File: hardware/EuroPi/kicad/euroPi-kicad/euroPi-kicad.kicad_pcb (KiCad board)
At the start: 2 copper layers, 121.9 x 128.5 mm, 104 parts, among them J1 Output 1 Jack, J10 Eurorack Power 2x8 16p, J11 Conn_01x13_Socket, J12 OLED 64x128, J13 USB_B_Micro, J14 Conn_01x03_Pin, J15 Conn_01x04_Pin, J16 Conn_02x04_Top_Bottom, J17 Conn_01x13_Pin, J18 Conn_01x04_Pin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

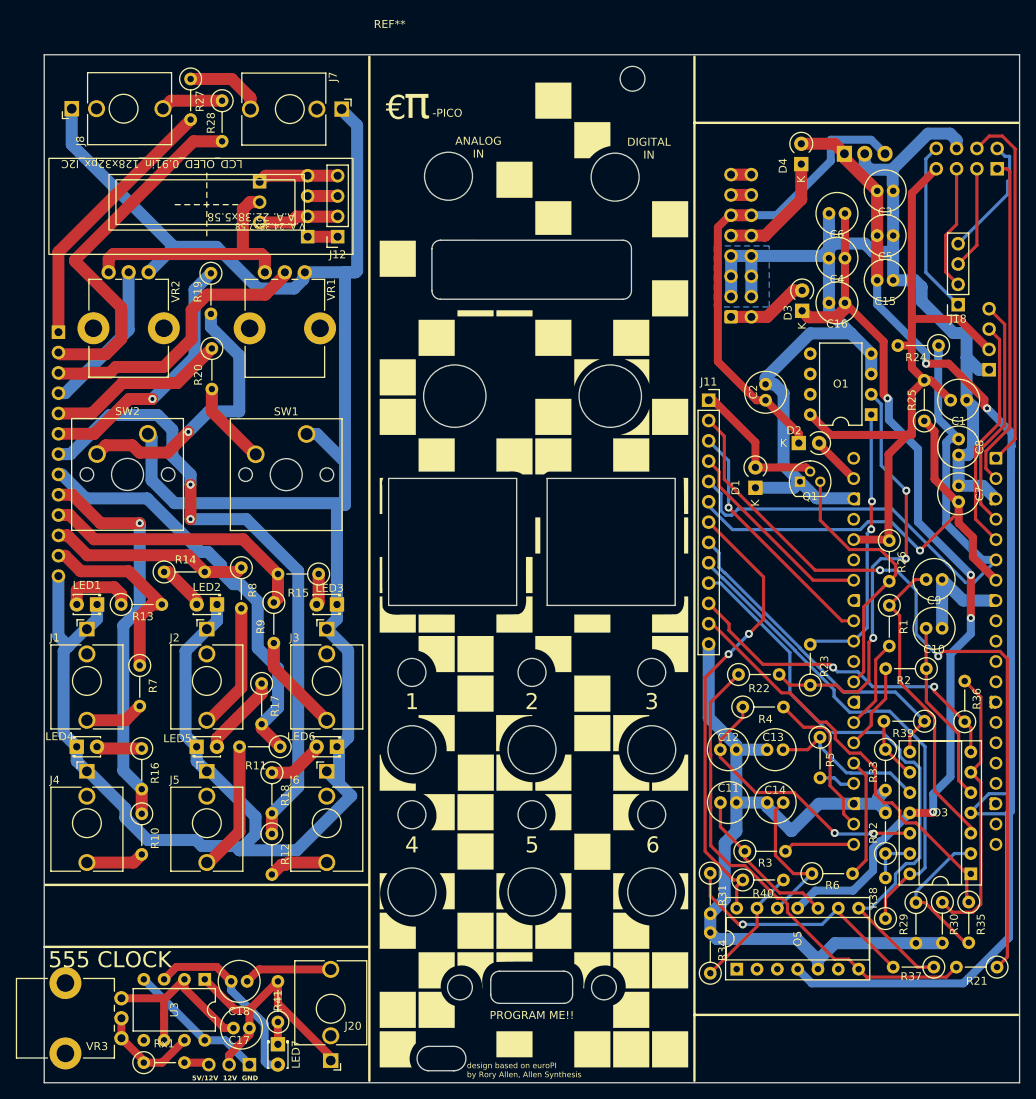
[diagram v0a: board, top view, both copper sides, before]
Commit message: euroPI base minor fixes incl adding ground plane
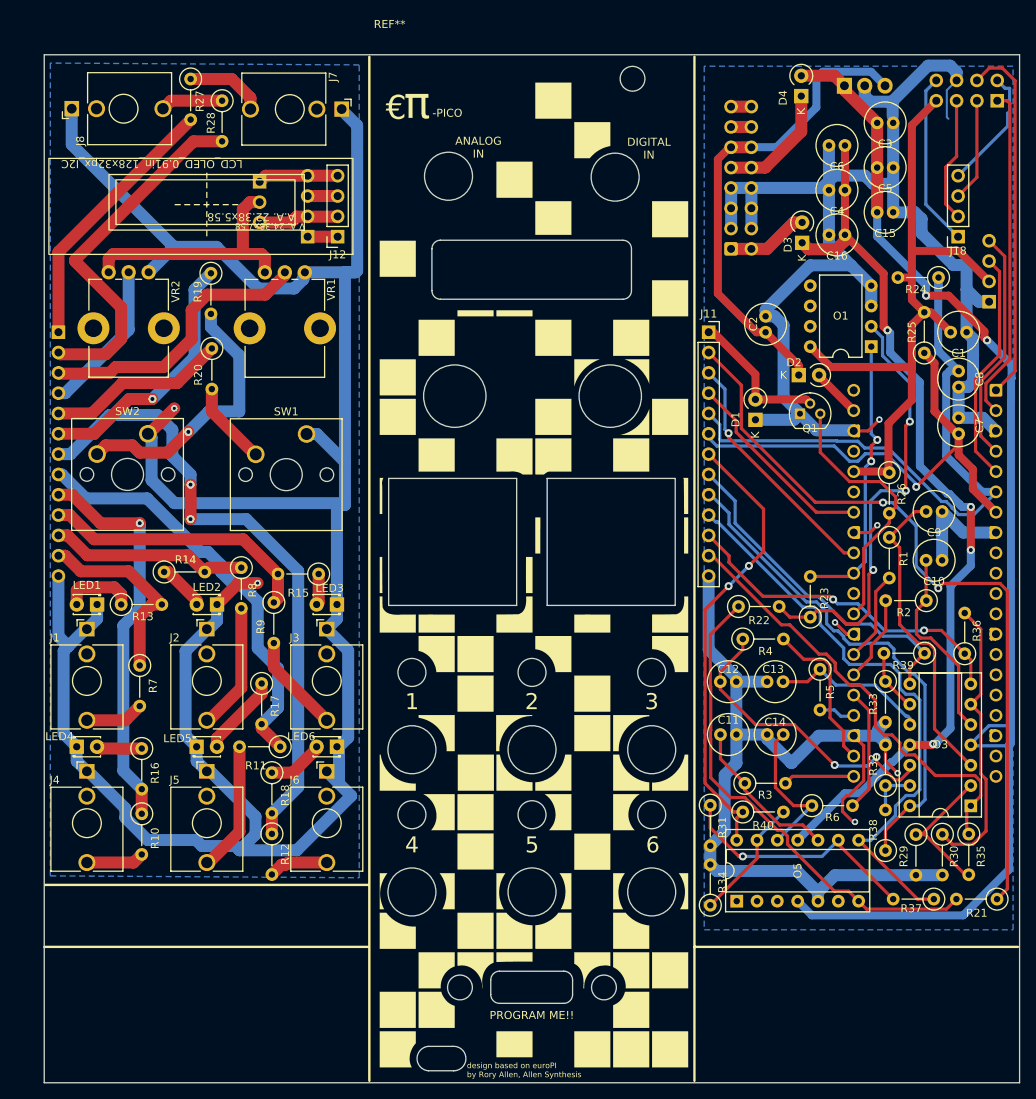
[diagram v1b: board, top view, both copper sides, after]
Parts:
- removed C17: 1uF, Capacitor_THT:C_Radial_D5.0mm_H11.0mm_P2.00mm
- removed C18: 10uF, Capacitor_THT:C_Radial_D5.0mm_H11.0mm_P2.00mm
- removed J20: Output 5 Jack, Connector_Audio:Jack_3.5mm_QingPu_WQP-PJ398SM_Vertical_CircularHoles
- removed J21: Conn_01x03_Pin, Connector_PinSocket_2.54mm:PinSocket_1x03_P2.54mm_Vertical
- removed LED7: LED, LED_THT:LED_D1.8mm_W3.3mm_H2.4mm
- removed R41, Rx1: 1K, Resistor_THT:R_Axial_DIN0207_L6.3mm_D2.5mm_P5.08mm_Vertical
- removed U3: LM555xN, Package_DIP:DIP-8_W7.62mm
- removed VR3: 10K, Potentiometer_THT:Potentiometer_Bourns_PTV09A-1_Single_Vertical
- moved R38 8.50 mm to (186.4, 124.9)
- moved R40 8.50 mm to (168.6, 120.1)
- moved R25 8.50 mm to (191.3, 62.7)
- moved D4 8.50 mm to (175.9, 30.6)
- moved U1 8.50 mm to (181.3, 29.3)
- moved C1 8.50 mm to (194.6, 60.1)
- moved C10 8.50 mm to (191.5, 88.6)
- moved C11 8.50 mm to (165.8, 110.4)
- moved C12 8.50 mm to (165.8, 103.8)
- moved C13 8.50 mm to (173.6, 103.8)
- moved C14 8.50 mm to (173.7, 110.4)
- moved C15 8.50 mm to (185.4, 45.1)
- moved C16 8.50 mm to (179.4, 47.9)
- moved C2 8.50 mm to (171.4, 60.1)
- moved C3 8.50 mm to (185.4, 33.9)
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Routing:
- net Net-(U3-THR): track 23.4 -> 0.00 mm
- net Net-(LED7-A): track 23.3 -> 0.00 mm
- net ~: track 172.5 -> 154.9 mm
- net Net-(U3-DIS): track 13.2 -> 0.00 mm
- net Net-(C18-Pad1): track 11.1 -> 0.00 mm
- net I2C_GND: track 610.0 -> 621.1 mm, vias 0 -> 7
- net CJ1: track 77.4 -> 81.0 mm
- net Net-(O3D-+): track 35.2 -> 38.3 mm
- net Net-(LED7-K): track 2.79 -> 0.00 mm
- net +5V: track 62.8 -> 60.3 mm
- net Net-(O3B-+): track 22.9 -> 24.6 mm
- net CJ4: track 111.3 -> 112.6 mm
- net Net-(O1A--): track 54.2 -> 55.4 mm
- net Net-(O3A--): track 18.9 -> 18.1 mm
- net Net-(O3A-+): track 38.6 -> 39.4 mm
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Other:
- board text removed: "555 CLOCK"
- board text removed: "5V/12V 12V GND"
- board text removed: "GND 12V 5V/12V"

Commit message: small fixes added missed net and text around eurorack conn
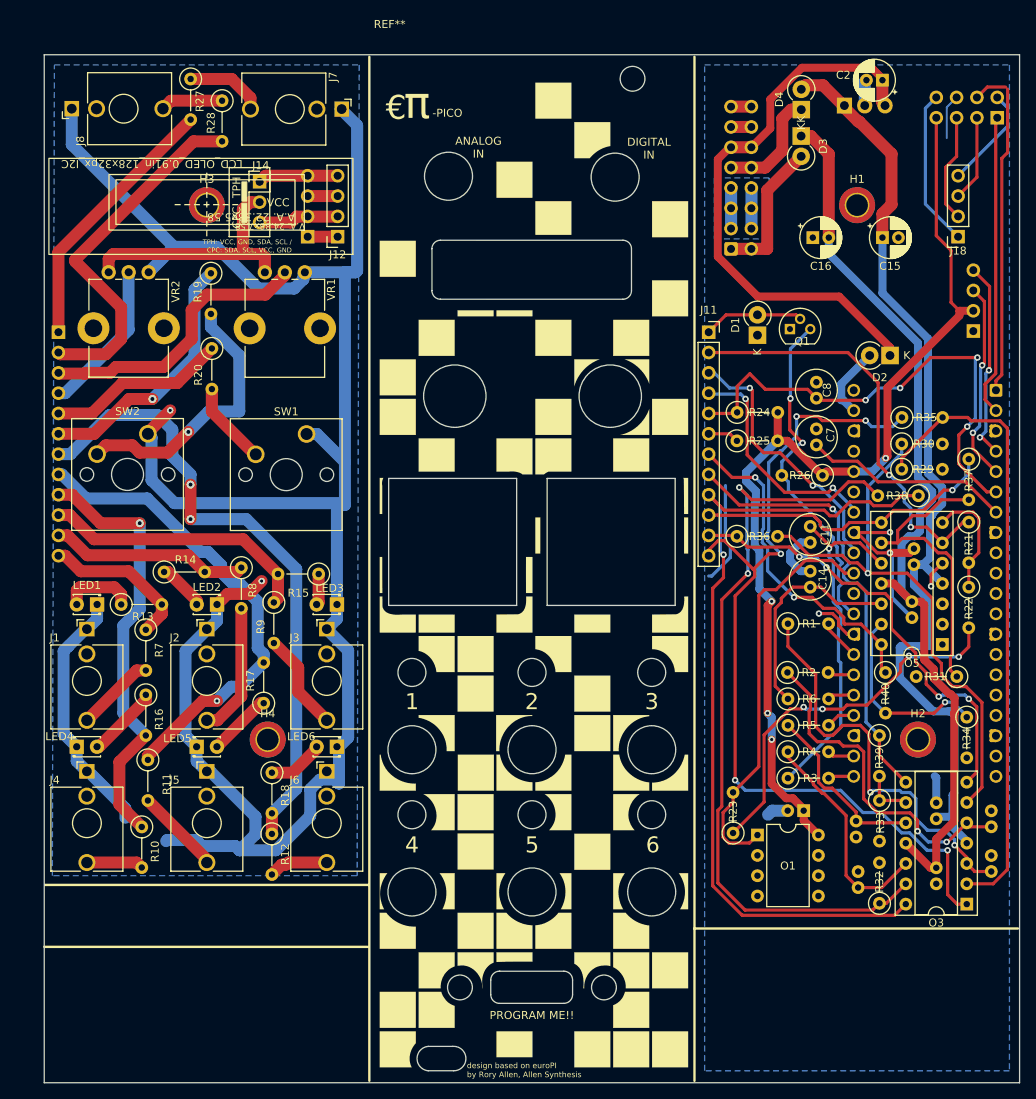
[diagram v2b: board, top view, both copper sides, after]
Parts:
- added H1: MountingHole_Pad, MountingHole:MountingHole_2.7mm_M2.5_ISO14580_Pad_TopBottom, F.Cu at (182.9, 44.2)
- added H2: MountingHole_Pad, MountingHole:MountingHole_2.7mm_M2.5_ISO14580_Pad_TopBottom, F.Cu at (190.5, 111.0)
- added H3: MountingHole_Pad, MountingHole:MountingHole_2.7mm_M2.5_ISO14580_Pad_TopBottom, F.Cu at (101.6, 44.2)
- added H4: MountingHole_Pad, MountingHole:MountingHole_2.7mm_M2.5_ISO14580_Pad_TopBottom, F.Cu at (109.2, 111.0)
- C1: value 1uF -> 1uF (Polarised); footprint Capacitor_THT:C_Radial_D5.0mm_H11.0mm_P2.00mm -> Capacitor_THT:CP_Radial_D5.0mm_P2.00mm; moved to B.Cu
- C10, C12, C13, C3, C4, C5, C6, C9: moved to B.Cu
- C15, C16: value 10uF -> 10uF (Polarised); footprint Capacitor_THT:C_Radial_D5.0mm_H11.0mm_P2.00mm -> Capacitor_THT:CP_Radial_D5.0mm_P2.00mm
- C2: value 1uF -> 1uF (Polarised); footprint Capacitor_THT:C_Radial_D5.0mm_H11.0mm_P2.00mm -> Capacitor_THT:CP_Radial_D5.0mm_P2.00mm
- D1, D2, D3, D4: value type="D" model="DIODE" lib="" -> 1N5817 Schottky Diode; footprint Diode_THT:D_A-405_P2.54mm_Vertical_KathodeUp -> Diode_THT:D_DO-41_SOD81_P2.54mm_Vertical_KathodeUp
- J11: value Conn_01x13_Socket -> Conn_01x12_Socket; footprint Connector_PinSocket_2.54mm:PinSocket_1x13_P2.54mm_Vertical -> Connector_PinSocket_2.54mm:PinSocket_1x12_P2.54mm_Vertical
- J14: moved to F.Cu
- J17: value Conn_01x13_Pin -> Conn_01x12_Pin; footprint Connector_PinSocket_2.54mm:PinSocket_1x13_P2.54mm_Vertical -> Connector_PinHeader_2.54mm:PinHeader_1x12_P2.54mm_Vertical
- O3, O5: footprint Package_DIP:DIP-14_W7.62mm_Socket -> Library:DIP-14_W7.62mm_Socket_gap_in_the_middle
- moved C6 93.3 mm to (192.8, 129.0), turned to 90 degrees
- moved C5 81.7 mm to (192.8, 120.9), turned to 90 degrees
- moved O1 62.7 mm to (170.4, 122.9), turned to 0 degrees
- moved C1 62.6 mm to (176.2, 119.9), turned to 180 degrees
- moved C3 55.4 mm to (190.0, 89.1), turned to 90 degrees
- moved R37 55.2 mm to (196.8, 75.9), turned to -90 degrees
- moved C4 54.4 mm to (189.7, 95.8), turned to 90 degrees
- moved R35 52.7 mm to (188.5, 70.7), turned to 0 degrees
- moved R30 49.1 mm to (188.5, 74.0), turned to 0 degrees
- moved R21 47.3 mm to (196.8, 83.8), turned to -90 degrees
- moved C9 45.7 mm to (199.7, 127.5), turned to 90 degrees
- moved R29 45.7 mm to (188.5, 77.2), turned to 0 degrees
- moved R38 44.5 mm to (190.6, 80.5), turned to 180 degrees
- moved O5 41.1 mm to (193.5, 99.1), turned to 180 degrees
- moved R34 39.7 mm to (196.6, 108.2), turned to -90 degrees
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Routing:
- net I2C_GND: track 621.1 -> 366.6 mm, vias 7 -> 6
- net Net-(O3D--): track 6.10 -> 97.3 mm, vias 0 -> 2
- net Net-(O3A--): track 18.1 -> 78.2 mm
- net CJ1: track 81.0 -> 131.6 mm, vias 0 -> 5
- net Net-(O5-Pad7): track 61.5 -> 14.6 mm
- net CJ4: track 112.6 -> 159.3 mm, vias 1 -> 2
- net CJA: track 140.8 -> 97.2 mm
- net I2C_VCC: track 117.6 -> 156.1 mm, vias 0 -> 4
- net CJ3: track 107.5 -> 72.5 mm, vias 0 -> 1
- net Net-(O3B--): track 36.0 -> 70.4 mm, vias 0 -> 1
- net CS2: track 94.8 -> 62.1 mm, vias 2 -> 1
- net ~: track 154.9 -> 123.3 mm, vias 2 -> 0
- net Net-(O5C-+): track 20.0 -> 44.0 mm, vias 0 -> 1
- net CJ5: track 95.5 -> 116.2 mm, vias 0 -> 2
- net Net-(O3B-+): track 24.6 -> 42.7 mm, vias 0 -> 2
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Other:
- board text added: "I2C"
